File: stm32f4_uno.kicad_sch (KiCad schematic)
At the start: 40 parts, among them J101 Digital/PWM, J102 Power, J103 Analog, J104 Digital/PWM, J4 Conn_ST_STDC14, U101 STM32F407VGTx, Y3 32.768kHz, Y4 25MHz

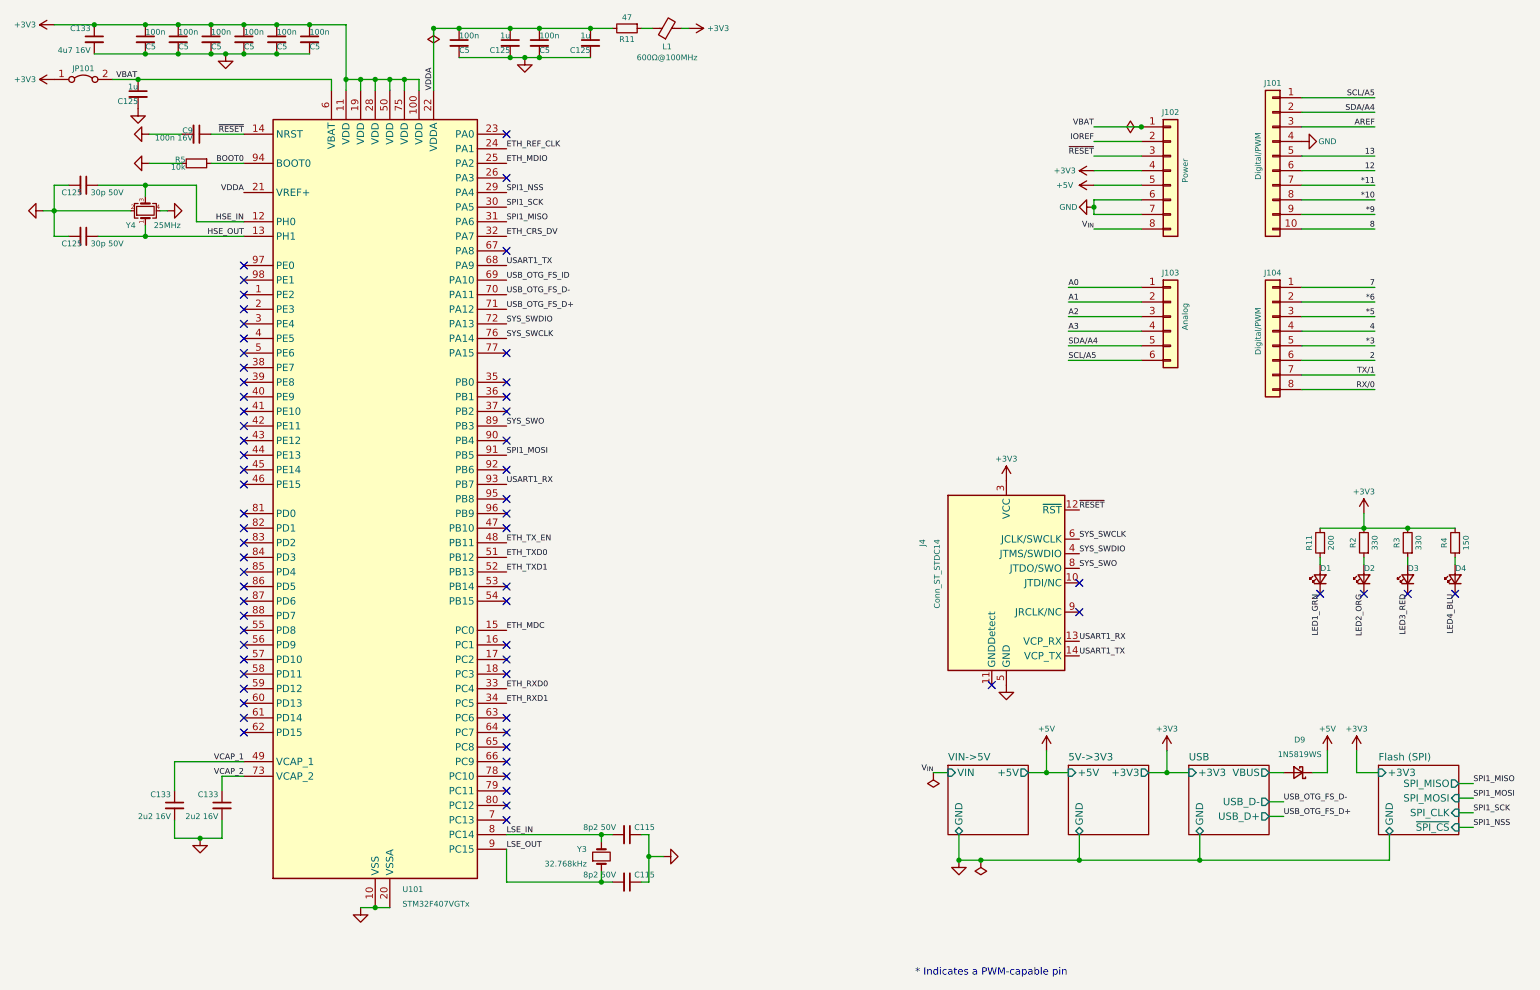
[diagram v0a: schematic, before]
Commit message: Finish schematic with all pins
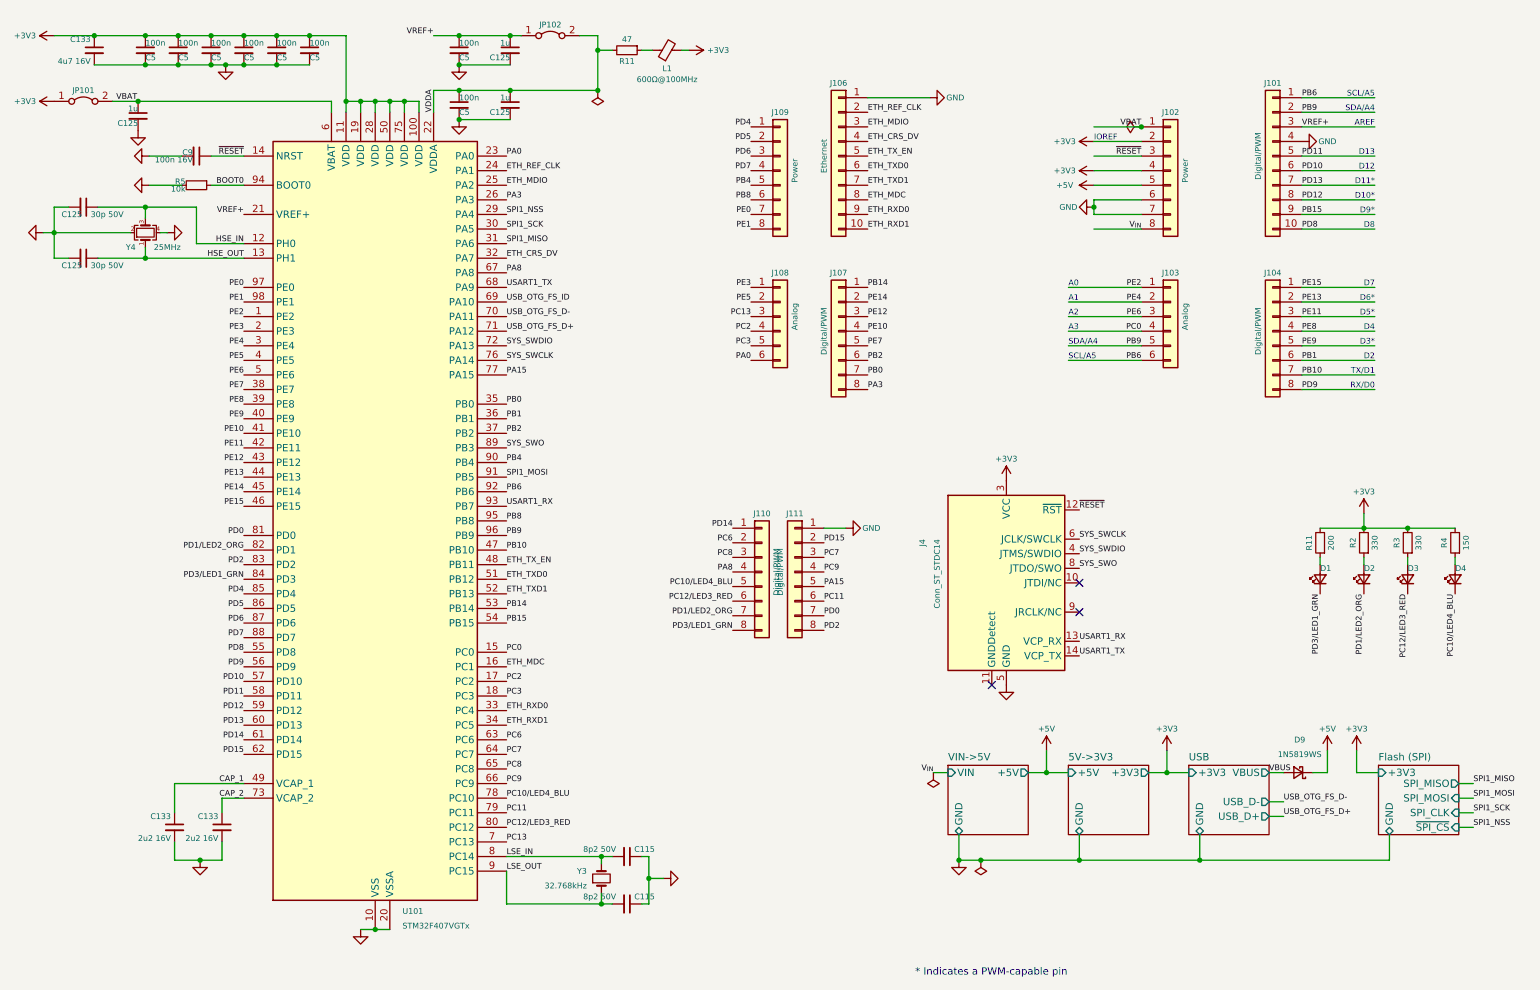
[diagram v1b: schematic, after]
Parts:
- added J106: Ethernet, Connector_PinSocket_2.54mm:PinSocket_1x10_P2.54mm_Vertical, symbol Connector_Generic:Conn_01x10
- added J107, J110, J111: Digital/PWM, Connector_PinSocket_2.54mm:PinSocket_1x08_P2.54mm_Vertical, symbol Connector_Generic:Conn_01x08
- added J108: Analog, Connector_PinSocket_2.54mm:PinSocket_1x06_P2.54mm_Vertical, symbol Connector_Generic:Conn_01x06
- added J109: Power, Connector_PinSocket_2.54mm:PinSocket_1x08_P2.54mm_Vertical, symbol Connector_Generic:Conn_01x08
- added JP102: Jumper_2_Bridged, Jumper:SolderJumper-2_P1.3mm_Bridged_RoundedPad1.0x1.5mm, symbol Jumper:Jumper_2_Bridged
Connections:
- net *10 is gone; now on net PD12: J101.8 (Pin_8)
- net *11 is gone; now on net PD13: J101.7 (Pin_7)
- net *3 is gone; now on net PE9: J104.5 (Pin_5)
- net *5 is gone; now on net PE11: J104.3 (Pin_3)
- net *6 is gone; now on net PE13: J104.2 (Pin_2)
- net *9 is gone; now on net PB15: J101.9 (Pin_9)
- net 12 is gone; now on net PD10: J101.6 (Pin_6)
- net 13 is gone; now on net PD11: J101.5 (Pin_5)
- net 2 is gone; now on net PB1: J104.6 (Pin_6)
- net 4 is gone; now on net PE8: J104.4 (Pin_4)
- net 7 is gone; now on net PE15: J104.1 (Pin_1)
- net 8 is gone; now on net PD8: J101.10 (Pin_10)
- net A0 is gone; now on net PE2: J103.1 (Pin_1)
- net A1 is gone; now on net PE4: J103.2 (Pin_2)
- net A2 is gone; now on net PE6: J103.3 (Pin_3)
- net IOREF is gone; now on net +3V3: J102.2 (Pin_2)
- net LED1_GRN is gone; now on net PD3/LED1_GRN: D1.1 (K)
- net LED2_ORG is gone; now on net PD1/LED2_ORG: D2.1 (K)
- net LED3_RED is gone; now on net PC12/LED3_RED: D3.1 (K)
- net LED4_BLU is gone; now on net PC10/LED4_BLU: D4.1 (K)
- net RX/0 is gone; now on net PD9: J104.8 (Pin_8)
- net SCL/A5 is gone; now on net PB6: J101.1 (Pin_1), J103.6 (Pin_6)
- net SDA/A4 is gone; now on net PB9: J101.2 (Pin_2), J103.5 (Pin_5)
- net TX/1 is gone; now on net PB10: J104.7 (Pin_7)
- net ETH_CRS_DV: now also J106.4 (Pin_4)
- net ETH_MDC: now also U101.16 (PC1), J106.8 (Pin_8); no longer U101.15 (PC0)
- net ETH_MDIO: now also J106.3 (Pin_3)
- net ETH_REF_CLK: now also J106.2 (Pin_2)
- net ETH_RXD0: now also J106.9 (Pin_9)
- net ETH_RXD1: now also J106.10 (Pin_10)
- net ETH_TXD0: now also J106.6 (Pin_6)
- net ETH_TXD1: now also J106.7 (Pin_7)
- net ETH_TX_EN: now also J106.5 (Pin_5)
- net GND: now also J106.1 (Pin_1), J111.1 (Pin_1)
- net VDDA: now also JP102.2 (B); no longer C125.1, C5.1, U101.21 (VREF+)
- net PE2: now reaches U101.1 (PE2)
- net PC2: now reaches U101.17 (PC2)
- net PC2: now also J108.4 (Pin_4)
- net PC3: now reaches U101.18 (PC3)
- net PC3: now also J108.5 (Pin_5)
- net PE3: now reaches U101.2 (PE3)
- net PE3: now also J108.1 (Pin_1)
- net PA0: now reaches U101.23 (PA0)
- net PA0: now also J108.6 (Pin_6)
- net PA3: now reaches U101.26 (PA3)
- net PA3: now also J107.8 (Pin_8)
- net PE4: now reaches U101.3 (PE4)
- net PB0: now reaches U101.35 (PB0)
- net PB0: now also J107.7 (Pin_7)
- net PB1: now reaches U101.36 (PB1)
- net PB2: now reaches U101.37 (PB2)
- net PB2: now also J107.6 (Pin_6)
- net PE7: now reaches U101.38 (PE7)
- net PE7: now also J107.5 (Pin_5)
- net PE8: now reaches U101.39 (PE8)
- net PE5: now reaches U101.4 (PE5)
- net PE5: now also J108.2 (Pin_2)
- net PE9: now reaches U101.40 (PE9)
- net PE10: now reaches U101.41 (PE10)
- net PE10: now also J107.4 (Pin_4)
- net PE11: now reaches U101.42 (PE11)
- net PE12: now reaches U101.43 (PE12)
- net PE12: now also J107.3 (Pin_3)
- net PE13: now reaches U101.44 (PE13)
- net PE14: now reaches U101.45 (PE14)
- net PE14: now also J107.2 (Pin_2)
- net PE15: now reaches U101.46 (PE15)
- net PB10: now reaches U101.47 (PB10)
- net PE6: now reaches U101.5 (PE6)
- net PB14: now reaches U101.53 (PB14)
- net PB14: now also J107.1 (Pin_1)
- net PB15: now reaches U101.54 (PB15)
- net PD8: now reaches U101.55 (PD8)
- net PD9: now reaches U101.56 (PD9)
- net PD10: now reaches U101.57 (PD10)
- net PD11: now reaches U101.58 (PD11)
- net PD12: now reaches U101.59 (PD12)
- net PD13: now reaches U101.60 (PD13)
- net PD14: now reaches U101.61 (PD14)
- net PD14: now also J110.1 (Pin_1)
- net PD15: now reaches U101.62 (PD15)
- net PD15: now also J111.2 (Pin_2)
- net PC6: now reaches U101.63 (PC6)
- net PC6: now also J110.2 (Pin_2)
- net PC7: now reaches U101.64 (PC7)
- net PC7: now also J111.3 (Pin_3)
- net PC8: now reaches U101.65 (PC8)
- net PC8: now also J110.3 (Pin_3)
- net PC9: now reaches U101.66 (PC9)
- net PC9: now also J111.4 (Pin_4)
- net PA8: now reaches U101.67 (PA8)
- net PA8: now also J110.4 (Pin_4)
- net PC13: now reaches U101.7 (PC13)
- net PC13: now also J108.3 (Pin_3)
- net PA15: now reaches U101.77 (PA15)
- net PA15: now also J111.5 (Pin_5)
- net PC10/LED4_BLU: now reaches U101.78 (PC10)
- net PC10/LED4_BLU: now also J110.5 (Pin_5)
- net PC11: now reaches U101.79 (PC11)
- net PC11: now also J111.6 (Pin_6)
- net PC12/LED3_RED: now reaches U101.80 (PC12)
- net PC12/LED3_RED: now also J110.6 (Pin_6)
- net PD0: now reaches U101.81 (PD0)
- net PD0: now also J111.7 (Pin_7)
- net PD1/LED2_ORG: now reaches U101.82 (PD1)
- net PD1/LED2_ORG: now also J110.7 (Pin_7)
- net PD2: now reaches U101.83 (PD2)
- net PD2: now also J111.8 (Pin_8)
- net PD3/LED1_GRN: now reaches U101.84 (PD3)
- net PD3/LED1_GRN: now also J110.8 (Pin_8)
- net PD4: now reaches U101.85 (PD4)
- net PD4: now also J109.1 (Pin_1)
- net PD5: now reaches U101.86 (PD5)
- net PD5: now also J109.2 (Pin_2)
- net PD6: now reaches U101.87 (PD6)
- net PD6: now also J109.3 (Pin_3)
- net PD7: now reaches U101.88 (PD7)
- net PD7: now also J109.4 (Pin_4)
- net PB4: now reaches U101.90 (PB4)
- net PB4: now also J109.5 (Pin_5)
- net PB6: now reaches U101.92 (PB6)
- net PB8: now reaches U101.95 (PB8)
- net PB8: now also J109.6 (Pin_6)
- net PB9: now reaches U101.96 (PB9)
- net PE0: now reaches U101.97 (PE0)
- net PE0: now also J109.7 (Pin_7)
- net PE1: now reaches U101.98 (PE1)
- net PE1: now also J109.8 (Pin_8)
- net A3 renamed PC0
- net PC0: now also U101.15 (PC0)
- net AREF renamed VREF+
- net VREF+: now also C125.1, C5.1, U101.21 (VREF+), JP102.1 (A)
- net USB/VBUS renamed VBUS
- net VCAP_1 renamed CAP_1
- net VCAP_2 renamed CAP_2
- no-connect marks 64 -> 3
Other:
- note added: "A0"
- note added: "A1"
- note added: "A2"
- note added: "A3"
- note added: "AREF"
- note added: "D10*"
- note added: "D11*"
- note added: "D12"
- note added: "D13"
- note added: "D2"
- note added: "D3*"
- note added: "D4"
- note added: "D5*"
- note added: "D6*"
- note added: "D7"
- note added: "D8"
- note added: "D9*"
- note added: "IOREF"
- note added: "RX/D0"
- note added: "SCL/A5"
- note added: "SDA/A4"
- note added: "TX/D1"
- moved on the sheet: C115, C125, C133, C5, C9, JP101, L1, R11, R5, U101, Y3, Y4

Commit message: WIP
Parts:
- added J1: Barrel_Jack, Connector_BarrelJack:BarrelJack_CUI_PJ-102AH_Horizontal, symbol Connector:Barrel_Jack
- J4: footprint Connector_Samtec:Samtec_FTSH-107-XX-YYY-DV-K-A -> Project_Library:Samtec_FTSH-107-XX-YYY-DV-K; now not fitted; now left out of the parts list
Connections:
- net ETH_CRS_DV: now also J106.7 (Pin_7); no longer J106.4 (Pin_4)
- net ETH_MDC: now also J106.10 (Pin_10); no longer J106.8 (Pin_8)
- net ETH_MDIO: now also J106.8 (Pin_8); no longer J106.3 (Pin_3)
- net ETH_REF_CLK: now also J106.9 (Pin_9); no longer J106.2 (Pin_2)
- net ETH_RXD0: now also J106.6 (Pin_6); no longer J106.9 (Pin_9)
- net ETH_RXD1: now also J106.5 (Pin_5); no longer J106.10 (Pin_10)
- net ETH_TXD0: now also J106.3 (Pin_3); no longer J106.6 (Pin_6)
- net ETH_TXD1: now also J106.2 (Pin_2); no longer J106.7 (Pin_7)
- net ETH_TX_EN: now also J106.4 (Pin_4); no longer J106.5 (Pin_5)
- net GND: now also J1.2
- net PC0: now also J108.4 (Pin_4); no longer J103.4 (Pin_4)
- net PC13: now also J103.3 (Pin_3); no longer J108.3 (Pin_3)
- net PC2: now also J103.4 (Pin_4); no longer J108.4 (Pin_4)
- net PE2: now also J108.1 (Pin_1); no longer J103.1 (Pin_1)
- net PE3: now also J103.1 (Pin_1); no longer J108.1 (Pin_1)
- net PE4: now also J108.2 (Pin_2); no longer J103.2 (Pin_2)
- net PE5: now also J103.2 (Pin_2); no longer J108.2 (Pin_2)
- net PE6: now also J108.3 (Pin_3); no longer J103.3 (Pin_3)
- net V_{IN}: now also J1.1
- no-connect marks 3 -> 4
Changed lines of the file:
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@@
   (junction (at 107.315 16.51) (diameter 0) (color 0 0 0 0)
   )
+  (junction (at 180.975 144.78) (diameter 0) (color 0 0 0 0)
+  )
   (junction (at 107.315 26.035) (diameter 0) (color 0 0 0 0)
   )
@@
   )
   (no_connect (at 206.375 111.76))
+  (no_connect (at 106.68 62.865))
   (no_connect (at 191.135 129.54))
   (no_connect (at 206.375 116.84))
@@
     (stroke (width 0) (type default))
   )
+  (wire (pts (xy 172.72 160.02) (xy 185.42 160.02))
+    (stroke (width 0) (type default))
+  )
   (wire (pts (xy 34.925 16.51) (xy 43.815 16.51))
     (stroke (width 0) (type default))
@@
     (stroke (width 0) (type solid))
   )
+  (wire (pts (xy 172.72 144.78) (xy 180.975 144.78))
+    (stroke (width 0) (type default))
+  )
   (wire (pts (xy 88.9 27.94) (xy 86.36 27.94))
     (stroke (width 0) (type default))
@@
     (stroke (width 0) (type default))
   )
+  (wire (pts (xy 172.72 149.86) (xy 172.72 160.02))
+    (stroke (width 0) (type default))
+  )
   (wire (pts (xy 218.44 144.78) (xy 221.615 144.78))
     (stroke (width 0) (type default))
@@
     (effects (font (size 1 1)) (justify left bottom))
   )
-  (label "PE5" (at 149.225 62.865 180) (fields_autoplaced)
+  (label "PE5" (at 217.17 62.865 180) (fields_autoplaced)
     (effects (font (size 1 1)) (justify right bottom))
   )
@@
     (effects (font (size 1 1)) (justify right bottom))
   )
-  (label "PE4" (at 217.17 62.865 180) (fields_autoplaced)
+  (label "PE4" (at 149.225 62.865 180) (fields_autoplaced)
     (effects (font (size 1 1)) (justify right bottom))
   )
@@
     (effects (font (size 1 1)) (justify left bottom))
   )
-  (label "PC13" (at 149.225 65.405 180) (fields_autoplaced)
+  (label "PC13" (at 217.17 65.405 180) (fields_autoplaced)
     (effects (font (size 1 1)) (justify right bottom))
   )
@@
     (effects (font (size 1 1)) (justify left bottom))
   )
-  (label "ETH_MDIO" (at 169.545 32.385 0) (fields_autoplaced)
+  (label "ETH_MDIO" (at 169.545 45.085 0) (fields_autoplaced)
     (effects (font (size 1 1)) (justify left bottom))
   )
@@
     (effects (font (size 1 1)) (justify left bottom))
   )
-  (label "ETH_TXD1" (at 169.545 42.545 0) (fields_autoplaced)
+  (label "ETH_TXD1" (at 169.545 29.845 0) (fields_autoplaced)
     (effects (font (size 1 1)) (justify left bottom))
   )
@@
     (effects (font (size 1 1)) (justify right bottom))
   )
-  (label "ETH_MDC" (at 169.545 45.085 0) (fields_autoplaced)
+  (label "ETH_MDC" (at 169.545 50.165 0) (fields_autoplaced)
     (effects (font (size 1 1)) (justify left bottom))
   )
@@
     (effects (font (size 1 1)) (justify right bottom))
   )
-  (label "ETH_RXD0" (at 169.545 47.625 0) (fields_autoplaced)
+  (label "ETH_RXD0" (at 169.545 40.005 0) (fields_autoplaced)
     (effects (font (size 1 1)) (justify left bottom))
   )
@@
     (effects (font (size 1 1)) (justify right bottom))
   )
-  (label "PC0" (at 217.17 67.945 180) (fields_autoplaced)
+  (label "PC0" (at 149.225 67.945 180) (fields_autoplaced)
     (effects (font (size 1 1)) (justify right bottom))
   )
@@
     (effects (font (size 1 1)) (justify left bottom))
   )
-  (label "PE6" (at 217.17 65.405 180) (fields_autoplaced)
+  (label "PE6" (at 149.225 65.405 180) (fields_autoplaced)
     (effects (font (size 1 1)) (justify right bottom))
   )
@@
     (effects (font (size 1 1)) (justify left bottom))
   )
-  (label "PE3" (at 149.225 60.325 180) (fields_autoplaced)
+  (label "PE3" (at 217.17 60.325 180) (fields_autoplaced)
     (effects (font (size 1 1)) (justify right bottom))
   )
@@
     (effects (font (size 1 1)) (justify left bottom))
   )
-  (label "ETH_CRS_DV" (at 169.545 34.925 0) (fields_autoplaced)
+  (label "ETH_CRS_DV" (at 169.545 42.545 0) (fields_autoplaced)
     (effects (font (size 1 1)) (justify left bottom))
   )
@@
     (effects (font (size 1 1)) (justify right bottom))
   )
-  (label "ETH_REF_CLK" (at 169.545 29.845 0) (fields_autoplaced)
+  (label "ETH_REF_CLK" (at 169.545 47.625 0) (fields_autoplaced)
     (effects (font (size 1 1)) (justify left bottom))
   )
@@
     (effects (font (size 1 1)) (justify left bottom))
   )
-  (label "PE2" (at 217.17 60.325 180) (fields_autoplaced)
+  (label "PE2" (at 149.225 60.325 180) (fields_autoplaced)
     (effects (font (size 1 1)) (justify right bottom))
   )
@@
     (effects (font (size 1 1)) (justify right bottom))
   )
-  (label "ETH_TX_EN" (at 169.545 37.465 0) (fields_autoplaced)
+  (label "ETH_TX_EN" (at 169.545 34.925 0) (fields_autoplaced)
     (effects (font (size 1 1)) (justify left bottom))
   )
@@
     (effects (font (size 1 1)) (justify right bottom))
   )
-  (label "ETH_RXD1" (at 169.545 50.165 0) (fields_autoplaced)
+  (label "ETH_RXD1" (at 169.545 37.465 0) (fields_autoplaced)
     (effects (font (size 1 1)) (justify left bottom))
   )
@@
     (effects (font (size 1 1)) (justify right bottom))
   )
-  (label "ETH_TXD0" (at 169.545 40.005 0) (fields_autoplaced)
+  (label "ETH_TXD0" (at 169.545 32.385 0) (fields_autoplaced)
     (effects (font (size 1 1)) (justify left bottom))
   )
@@
     (effects (font (size 1 1)) (justify left bottom))
   )
-  (label "PC2" (at 149.225 67.945 180) (fields_autoplaced)
+  (label "PC2" (at 217.17 67.945 180) (fields_autoplaced)
     (effects (font (size 1 1)) (justify right bottom))
   )
@@
     (effects (font (size 1 1)) (justify left bottom))
   )
+  (netclass_flag "" (length 2.54) (shape round) (at 130.81 19.05 0) (fields_autoplaced)
+    (effects (font (size 1.27 1.27)) (justify left bottom))
+    (property "Netclass" "Power" (at 131.699 16.51 0)
+      (effects (font (size 1.27 1.27) italic) (justify left))
+    )
+  )
   (symbol (lib_id "Connector_Generic:Conn_01x08") (at 222.25 40.005 0) (unit 1)
     (in_bom yes) (on_board yes) (dnp no)
@@
     )
   )
+  (symbol (lib_id "Connector:Barrel_Jack") (at 165.1 147.32 0) (unit 1)
+    (in_bom no) (on_board yes) (dnp yes) (fields_autoplaced)
+    (property "Reference" "J1" (at 165.1 139.065 0)
+      (effects (font (size 1.27 1.27)))
+    )
+    (property "Value" "Barrel_Jack" (at 165.1 141.605 0)
+      (effects (font (size 1.27 1.27)))
+    )
+    (property "Footprint" "Connector_BarrelJack:BarrelJack_CUI_PJ-102AH_Horizontal" (at 166.37 148.336 0)
+      (effects (font (size 1.27 1.27)) hide)
+    )
+    (property "Datasheet" "~" (at 166.37 148.336 0)
+      (effects (font (size 1.27 1.27)) hide)
+    )
+    (property "Description" "" (at 165.1 147.32 0)
+      (effects (font (size 1.27 1.27)) hide)
+    )
+    (property "Manufacturer" "" (at 165.1 147.32 0)
+      (effects (font (size 1.27 1.27)) hide)
+    )
+    (property "Partnumber" "" (at 165.1 147.32 0)
+      (effects (font (size 1.27 1.27)) hide)
+    )
+    (property "JLCPCB Part #" "" (at 165.1 147.32 0)
+      (effects (font (size 1.27 1.27)) hide)
+    )
+    (property "isBasicPart" "" (at 165.1 147.32 0)
+      (effects (font (size 1.27 1.27)) hide)
+    )
+    (pin "1")
+    (pin "2")
+    (instances
+      (project "stm32f4_uno"
+        (path "/e63e39d7-6ac0-4ffd-8aa3-1841a4541b55"
+          (reference "J1") (unit 1)
+        )
+      )
+    )
+  )
   (symbol (lib_id "Device:LED_Small") (at 263.525 111.125 90) (unit 1)
     (in_bom yes) (on_board yes) (dnp no)
@@
       (effects (font (size 1 1)) hide)
     )
-    (property "Datasheet" "https://datasheet.lcsc.com/lcsc/2303071500_Seiko-Epson-Q13FC1350004900_C95361.pdf" (at 123.19 163.195 0)
+    (property "Datasheet" "~" (at 123.19 163.195 0)
       (effects (font (size 1 1)) hide)
     )
@@
   )
   (symbol (lib_id "Connector:Conn_ST_STDC14") (at 193.675 111.76 0) (unit 1)
-    (in_bom yes) (on_board yes) (dnp no)
+    (in_bom no) (on_board yes) (dnp yes)
     (property "Reference" "J4" (at 179.07 104.14 90)
       (effects (font (size 1 1)) (justify right))
@@
       (effects (font (size 1 1)) (justify right))
     )
-    (property "Footprint" "Connector_Samtec:Samtec_FTSH-107-XX-YYY-DV-K-A" (at 193.675 111.76 0)
+    (property "Footprint" "Project_Library:Samtec_FTSH-107-XX-YYY-DV-K" (at 193.675 111.76 0)
       (effects (font (size 1 1)) hide)
     )
